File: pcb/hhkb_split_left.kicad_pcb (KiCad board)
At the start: 2 copper layers, 140.4 x 97.4 mm, 74 parts, among them SW1 Esc, SW10 E, SW11 R, SW12 T, SW13 Ctrl, SW14 A, SW15 S, SW16 D, SW17 F, SW18 G, SW19 Shift, SW2 1, SW20 Z, SW21 X, SW22 C, SW23 V, SW24 B, SW25 Alt, SW26 Meta, SW27 L-Space, SW3 2, SW4 3, SW5 4, SW6 5, SW7 Tab, SW8 Q, SW9 W, U1 74LVC595

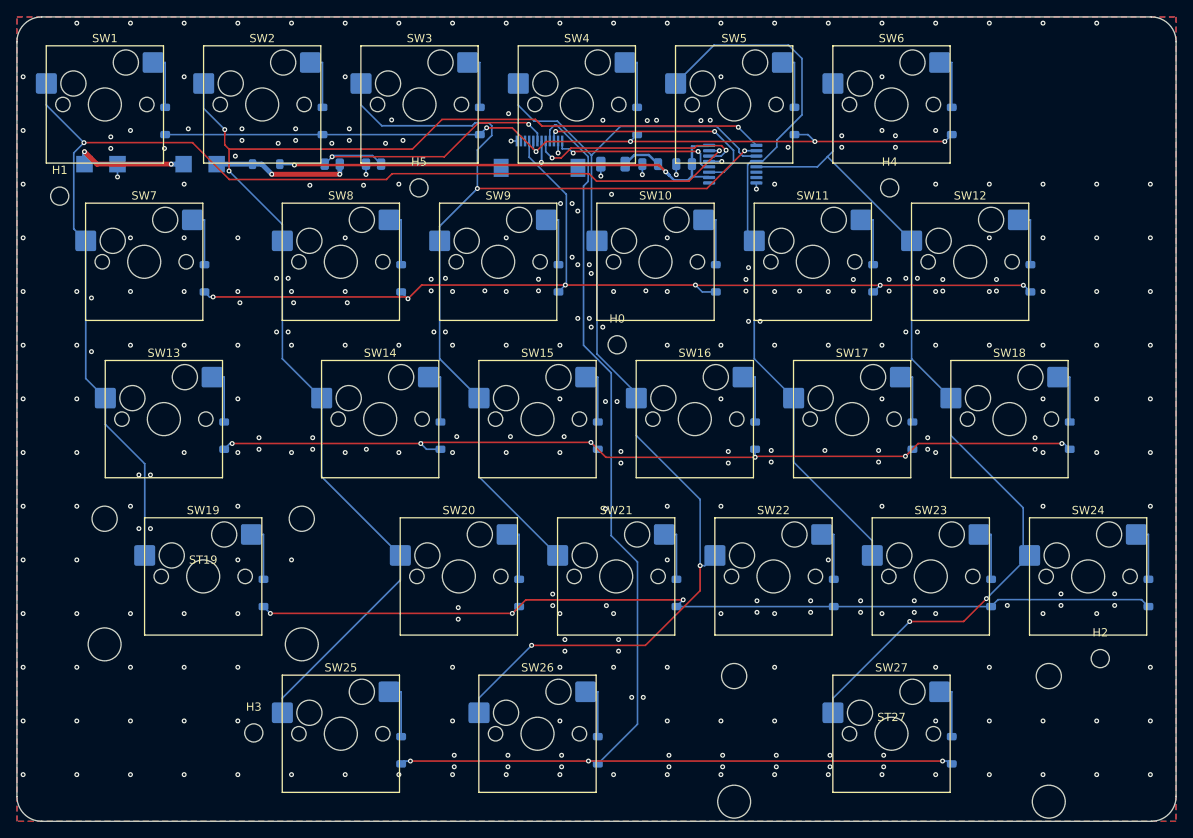
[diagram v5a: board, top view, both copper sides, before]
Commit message: 浮いた GND を 0 個にした。「消す」前に「繋ぐ」を尽くす（指摘 4/5）
利用者の指摘「0 は理想ではなく必達では。GND のレベルが違う可能性が
あるというのは致命的では」への対応。**指摘が正しく、私が誤っていた。**

私は「現実に 0 にできないので、増加を検出する用途に留める」と書いた。
これは事実に反する。**取り得る手は常に 2 つあり、どちらかは必ず選べる。**

  1. 繋ぐ  ビアが入るなら
  2. 消す  ビアが入らないなら、その銅を残す理由が無い

浮いた銅は電位が定義されておらず GND ではない。遮蔽の役に立たず、
囲んでいる配線どうしを容量結合させ、2.4GHz では再放射する。
**残す利益がゼロ**なので 0 を必達にした（MAX_FLOATING_ISLANDS = 0）。

★ その過程で、繋げるものまで捨てていたバグを 2 つ見つけた。

(1) **島の削除が先に走り、繋ぐ機会が無かった**
    ゾーンを ALWAYS にした結果、**塗った瞬間に浮いた区画が消える**。
    消えたあとに探しても見つからないので、離島に打ったビアは常に 0 だった。
    正しい順序に直した: 削除を止めて塗る → 置けるものにビアを打つ →
    削除を戻して塗る。**23.80mm²（3.76 x 9.75mm）の区画が救われた。**

(2) **探索が 0.5mm 刻みで、置ける場所を見落としていた**
    上記 23.80mm² には 0.1mm 刻みなら 512 点の置ける場所があった。

**刻みという調整値そのものを無くした。**標本化をやめ、幾何で解く。

    区画 − （障害物を「ビア半径＋クリアランス」だけ膨らませたもの）

残りが空でなければ置ける。空ならどうやっても置けない。
「細かく調べれば見つかるかも」が原理的に無くなる。

その実装でも 1 回間違えた。引き算のあとさらに区画の縁から Deflate して
おり、**クリアランスを二重に課していた**（標本化なら 24 点置ける区画を
「置けない」と誤判定）。ビアは区画の内側に丸ごと収まる必要が無い——
区画も GND、ビアも GND なので、守るべきは他ネットとの距離だけ。
直した結果、**45 区画すべてで幾何と標本化が一致（不一致 0）。**

最終状態:

    浮いた区画    左 0 個 / 右 0 個
    消した銅      左 28.4mm2（ベタの 0.13%）/ 右 57.5mm2（0.21%）
    離島に打ったビア 左 2 個 / 右 3 個

消したものは全て、幾何で「ビアが入らない」ことを証明済み。内訳は
スイッチ内部の 0.61x0.65mm の小片（約 30 個）と、幅 0.25〜0.7mm の
細長い帯。**ビアは直径 1.1mm 要るので物理的に入らない。**

Co-Authored-By: Claude Sonnet 5 <noreply@anthropic.com>
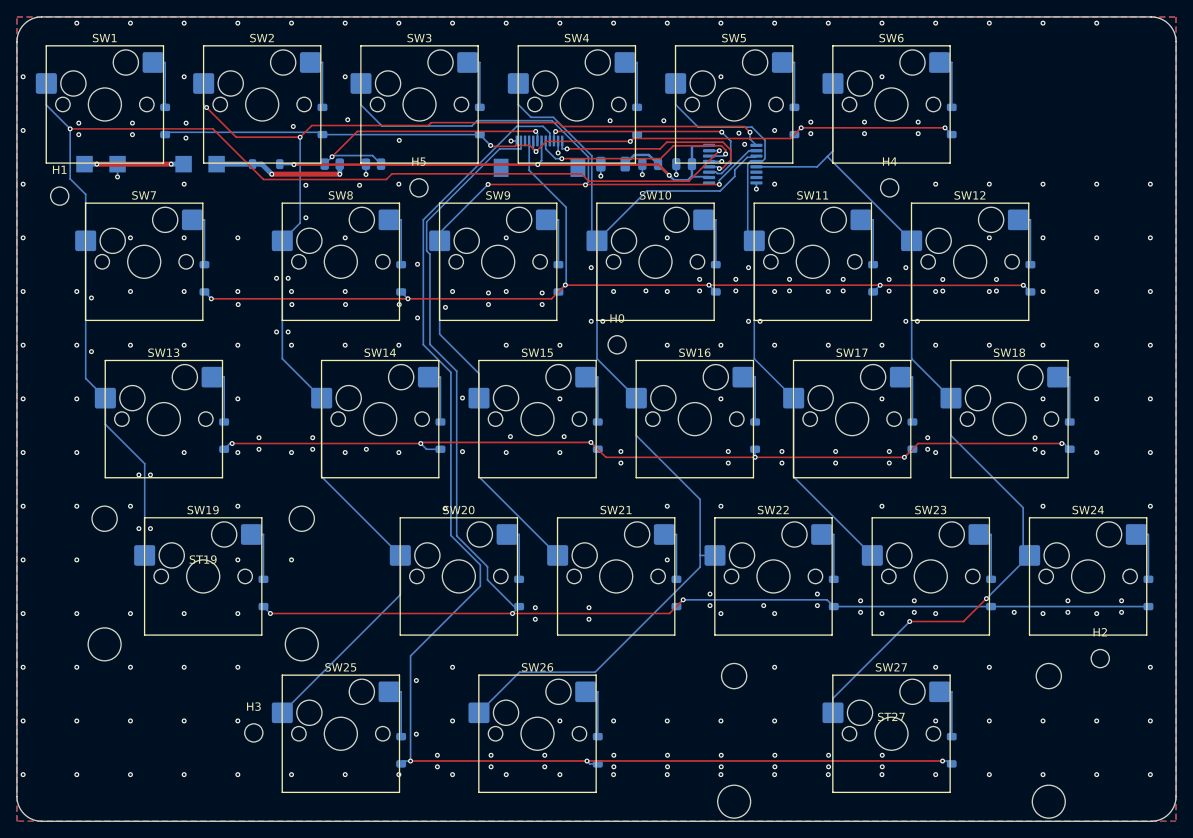
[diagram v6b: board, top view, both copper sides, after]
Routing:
- net ROW3: track 112.0 -> 178.3 mm
- net COL4: track 87.9 -> 73.4 mm
- net COL2: track 116.0 -> 124.6 mm, vias 2 -> 3
- net ROW4: track 154.5 -> 161.6 mm
- net CS: track 20.5 -> 26.5 mm
- net COL1: track 158.6 -> 155.9 mm
- net COL3: track 131.6 -> 129.2 mm, vias 2 -> 0
- net VBATT_RAW: track 14.1 -> 12.0 mm
- net ROW1: track 127.1 -> 125.4 mm
- net ROW0: track 103.1 -> 101.7 mm
- net COL0: track 145.3 -> 146.7 mm
- net VBATT_SENSE: track 35.7 -> 34.9 mm
- net GND: vias 343 -> 318

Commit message: ★ 斜めのバスにビアが 1 本も立っていなかった（指摘 5 が効いていなかった）
利用者が B.Cu の絵を見て「明らかに斜め線のところにビアがない」と指摘。
調べたら**私の実装に 3 つの欠陥**があった。どれも DRC では出ない。

**(1) 「長い配線」を線分 1 本の長さで判定していた**
列のバスのような斜めの経路は、キーごとの短い線分の連なりでできている。
COL0 は合計 152mm あるのに 10mm 以上の線分は 4 本しかない。
**全 406 本のうち 87%（355 本）が対象外**になっていた。
→ ネットが同じ面に持つ**経路の合計長**で見るようにした。

**(2) 配線を外接矩形で避けていた**
斜めの配線の外接矩形は対角線を含む巨大な長方形になる。つまり
**斜め線の周囲一帯が「置けない」**ことになり、一番ビアが要る場所に
1 本も立たなかった。格子のスティッチングが 8 割方失敗していたのも同じ原因。
→ 線分として点との距離で見るようにした（_near_segment）。

**(3) 順序が逆だった**
埋め草の格子を先に打っていたため、配線の脇という一番効く場所が
先取りされていた。→ 狙って打つフェンスを先に、格子を後に。

利用者の「配線は線分しかないのですか？色々曲がったりするでしょうに」で
**円弧（PCB_ARC）を黙って除外していた**ことも判明。いまの基板に円弧は
0 本（Freerouting は直線しか出さない）が、KiCad で手直しすれば生じる。
_as_segments が円弧を弦に割って扱うようにした。

結果（GND ビアの総数）:

    左  9 → **732 個**（うちフェンス 545）
    右 12 → **913 個**（うちフェンス 662）

DRC は 3 基板とも違反 0（右に 2 件出たのは Freerouting 自身の丸め。
DSN のクリアランスに 10µm 上乗せして解消済み）。

**編集を重ねた結果、gnd_fanout.py に関数が 9 個も二重定義されていた。**
後半が前半を上書きしていて動作はしていたが、重複を削除した。
使わなくなった widen も消した（CLAUDE.md「置き換えたら古い方を消す」）。

Co-Authored-By: Claude Sonnet 5 <noreply@anthropic.com>
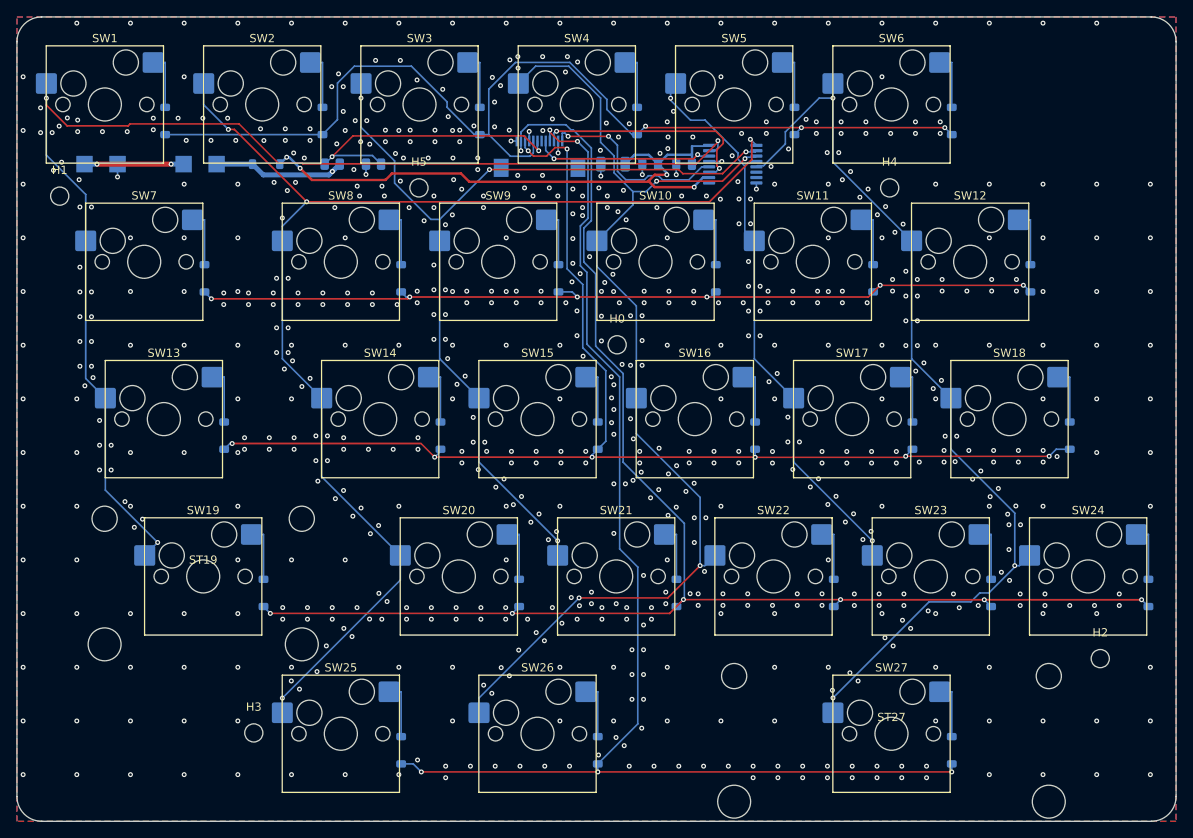
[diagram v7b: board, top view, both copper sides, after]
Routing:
- net ROW2: track 110.6 -> 153.9 mm, vias 6 -> 8
- net ROW0: track 101.7 -> 126.4 mm, vias 5 -> 3
- net ROW1: track 125.4 -> 108.9 mm, vias 6 -> 7
- net COL2: track 124.6 -> 109.8 mm, vias 3 -> 4
- net ROW3: track 178.3 -> 185.7 mm, vias 3 -> 7
- net ROW4: track 161.6 -> 155.6 mm, vias 3 -> 5
- net COL0: track 146.7 -> 152.0 mm, vias 2 -> 3
- net SPI_MOSI: track 26.7 -> 21.6 mm
- net V3V3: track 68.7 -> 73.1 mm, vias 3 -> 4
- net COL5: track 109.5 -> 113.9 mm, vias 2 -> 3
- net COL4: track 73.4 -> 70.2 mm, vias 0 -> 2
- net COL3: track 129.2 -> 131.9 mm, vias 0 -> 4
- net CS: track 26.5 -> 24.0 mm
- net COL1: track 155.9 -> 154.4 mm, vias 3 -> 4
- net SPI_SCK: track 28.9 -> 27.4 mm
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
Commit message: J_DBを帯またぎで子基板コネクタ直近へ移動（未配線 左0/右3 → 左1/右2）
利用者の提案「J_DBのX位置をDB基板コネクタに合わせる」の実験過程で、
帯0内での調整（全10案超）はすべて現状を上回れなかった。
「未配線数だけでなく、どのネットが毎回落ちるかを見る」提案を受けて
系統的に検証した結果、**帯をまたいでJ_DBを移動する**方向で改善した。

  左: J_DB (0,-6.9) → (1, 63.0)   未配線 0→0（維持、3回決定的に確認）
  右: J_DB (0,-23.5) → (1,-78.0)  未配線 3→1（改善、3回決定的に確認）

副産物として、FFCコネクタが子基板コネクタとほぼ同じX位置になった
（左: 差3.5mm、右: 差1.8mm）。子基板コネクタの中心Xは
gen_case.daughterboard_x_center（左+59.5mm/右-76.2mm）。

DSNクリアランスの上乗せ（Freeroutingが規則ぎりぎりを狙って丸め誤差で
僅かに下回る問題への対策）を10µm→25µmに調整。これによりDRC違反は
3基板とも0になったが、配線可能な余地を消費するトレードオフで
未配線が左0→1・右1→2に増えた。DRC違反0を優先して採用。

残る未配線3本（左1・右2）はどれも決定的に同じネットで再現する
（左: ROW0-J_DB、右: COL8-SW31＋GNDベタ浮島1件）。配置の揺れではなく
構造的な残り。

Co-Authored-By: Claude Sonnet 5 <noreply@anthropic.com>
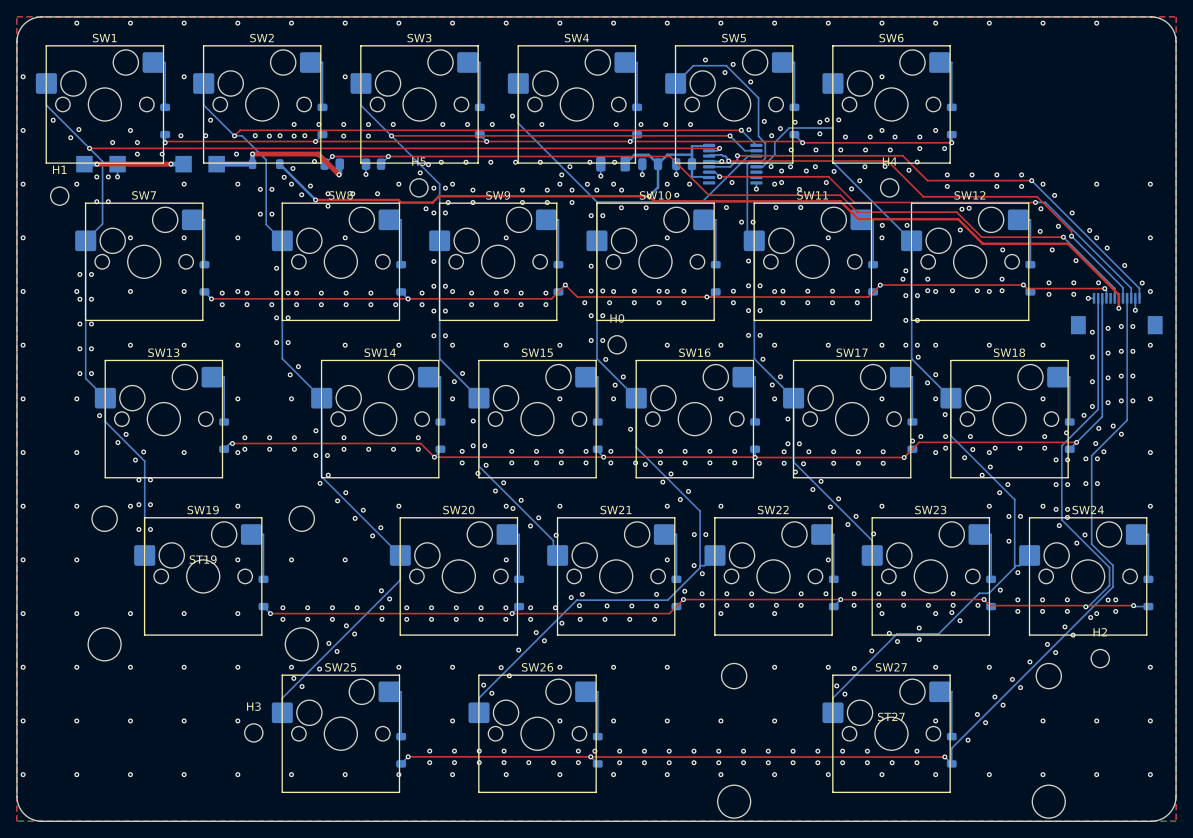
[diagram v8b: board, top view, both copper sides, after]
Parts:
- moved J_DB 72.4 mm to (213.0, 87.2)
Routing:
- net VBATT_SENSE: track 35.7 -> 105.2 mm, vias 2 -> 3
- net V3V3: track 73.1 -> 133.4 mm, vias 4 -> 3
- net SPI_MOSI: track 21.6 -> 58.6 mm
- net CS: track 24.0 -> 60.8 mm
- net SPI_SCK: track 27.4 -> 58.1 mm
- net ROW3: track 185.7 -> 156.4 mm
- net ROW2: track 153.9 -> 129.8 mm, vias 8 -> 6
- net ROW0: track 126.4 -> 102.3 mm, vias 3 -> 6
- net ROW4: track 155.6 -> 135.9 mm, vias 5 -> 3
- net COL0: track 152.0 -> 141.5 mm, vias 3 -> 2
- net ROW1: track 108.9 -> 118.8 mm
- net COL4: track 70.2 -> 76.3 mm, vias 2 -> 0
- net COL3: track 131.9 -> 126.8 mm, vias 4 -> 0
- net VBATT_SW: track 16.0 -> 18.4 mm, vias 1 -> 2
- net COL1: track 154.4 -> 156.8 mm, vias 4 -> 2
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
